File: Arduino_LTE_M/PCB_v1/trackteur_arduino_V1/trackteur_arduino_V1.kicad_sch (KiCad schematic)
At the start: 17 parts, among them J1 rPi_HDR, J2 DC/DC, J3 BATT_CAR, J4 MicroSD_Breakout, Q1 2N3904, U1 LD1117S33TR_SOT223

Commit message: update PCB
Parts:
- added H1, H2, H3: MountingHole, MountingHole:MountingHole_2.7mm_M2.5, symbol Mechanical:MountingHole
- added J5: Conn_02x02_Counter_Clockwise, Connector_PinHeader_2.54mm:PinHeader_2x02_P2.54mm_Vertical, symbol Connector_Generic:Conn_02x02_Counter_Clockwise
- added J6: Conn_01x06, Connector_PinHeader_2.54mm:PinHeader_1x06_P2.54mm_Vertical, symbol Connector_Generic:Conn_01x06
- added TP1: +5V, Connector_PinHeader_2.54mm:PinHeader_1x01_P2.54mm_Vertical, symbol Connector:TestPoint
- added TP2: GND, Connector_PinHeader_2.54mm:PinHeader_1x01_P2.54mm_Vertical, symbol Connector:TestPoint
- added TP3: +3.3V, Connector_PinHeader_2.54mm:PinHeader_1x01_P2.54mm_Vertical, symbol Connector:TestPoint
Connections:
- net +3.3V: now also TP3.1
- net +5V: now also J6.1 (Pin_1), TP1.1
- net GND: now also J6.6 (Pin_6), TP2.1
- net D7: now reaches A1.10 (D7)
- net D7: now also J6.4 (Pin_4)
- net D10: now reaches A1.13 (D10)
- net D10: now also J6.5 (Pin_5)
- net A0: now reaches A1.19 (A0)
- net A0: now also J5.4 (Pin_4)
- net A1: now reaches A1.20 (A1)
- net A1: now also J5.3 (Pin_3)
- net A2: now reaches A1.21 (A2)
- net A2: now also J5.2 (Pin_2)
- net A3: now reaches A1.22 (A3)
- net A3: now also J5.1 (Pin_1)
- net D5: now reaches A1.8 (D5)
- net D5: now also J6.2 (Pin_2)
- net D9: now reaches A1.9 (D6)
- net D9: now also J6.3 (Pin_3)

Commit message: Fichiers de fabrication
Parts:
- J3: footprint Connector_Wire:SolderWire-0.75sqmm_1x02_P7mm_D1.25mm_OD3.5mm -> Connector_Wire:SolderWire-2.5sqmm_1x02_P7.2mm_D2.4mm_OD3.6mm
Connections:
- net A0: now also J5.3 (Pin_3); no longer J5.4 (Pin_4)
- net A1: now also J5.4 (Pin_4); no longer J5.3 (Pin_3)
- net A2: now also J5.1 (Pin_1); no longer J5.2 (Pin_2)
- net A3: now also J5.2 (Pin_2); no longer J5.1 (Pin_1)
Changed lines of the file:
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@@
     )
   )
-  (global_label "A2" (shape bidirectional) (at 137.16 120.65 180) (fields_autoplaced)
+  (global_label "A3" (shape bidirectional) (at 137.16 120.65 180) (fields_autoplaced)
     (effects (font (size 1.27 1.27)) (justify right))
     (property "Intersheetrefs" "${INTERSHEET_REFS}" (at 130.7654 120.65 0)
@@
     )
   )
-  (global_label "A3" (shape bidirectional) (at 137.16 118.11 180) (fields_autoplaced)
+  (global_label "A2" (shape bidirectional) (at 137.16 118.11 180) (fields_autoplaced)
     (effects (font (size 1.27 1.27)) (justify right))
     (property "Intersheetrefs" "${INTERSHEET_REFS}" (at 130.7654 118.11 0)
@@
     )
   )
-  (global_label "A0" (shape bidirectional) (at 149.86 118.11 0) (fields_autoplaced)
+  (global_label "A1" (shape bidirectional) (at 149.86 118.11 0) (fields_autoplaced)
     (effects (font (size 1.27 1.27)) (justify left))
     (property "Intersheetrefs" "${INTERSHEET_REFS}" (at 156.2546 118.11 0)
@@
     )
   )
-  (global_label "A1" (shape bidirectional) (at 149.86 120.65 0) (fields_autoplaced)
+  (global_label "A0" (shape bidirectional) (at 149.86 120.65 0) (fields_autoplaced)
     (effects (font (size 1.27 1.27)) (justify left))
     (property "Intersheetrefs" "${INTERSHEET_REFS}" (at 156.2546 120.65 0)
@@
       (effects (font (size 1.27 1.27)))
     )
-    (property "Footprint" "Connector_Wire:SolderWire-0.75sqmm_1x02_P7mm_D1.25mm_OD3.5mm" (at 26.67 41.91 0)
-      (effects (font (size 1.27 1.27)) hide)
-    )
+    (property "Footprint" "Connector_Wire:SolderWire-2.5sqmm_1x02_P7.2mm_D2.4mm_OD3.6mm" (at 26.67 41.91 0)
+      (effects (font (size 1.27 1.27)) hide)
+    )

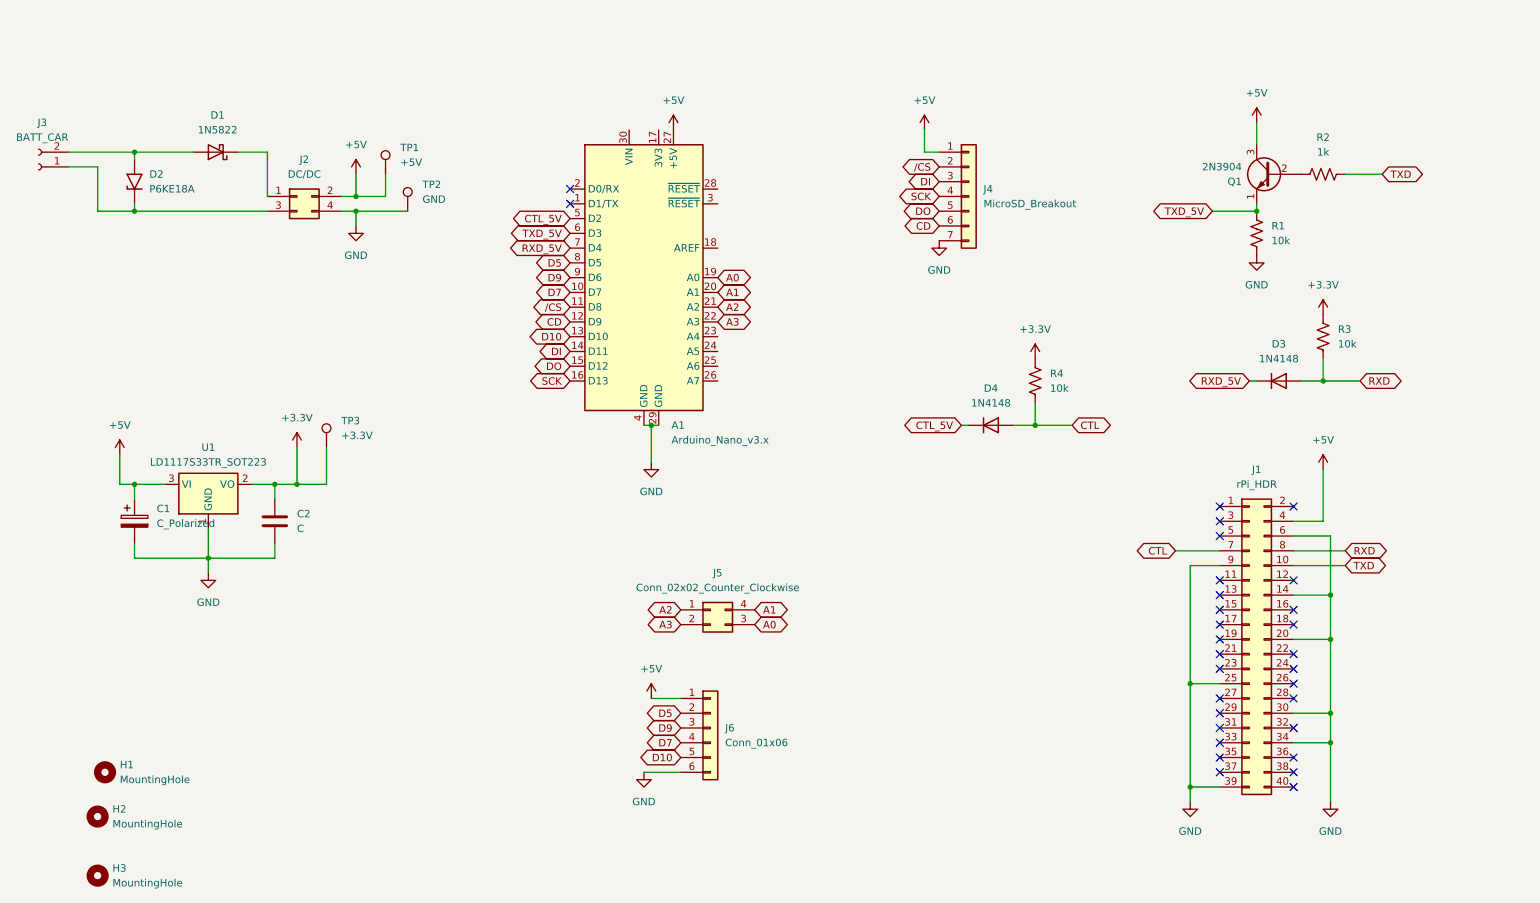
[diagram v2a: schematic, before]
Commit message: LTE send dummy gps working and new pcb
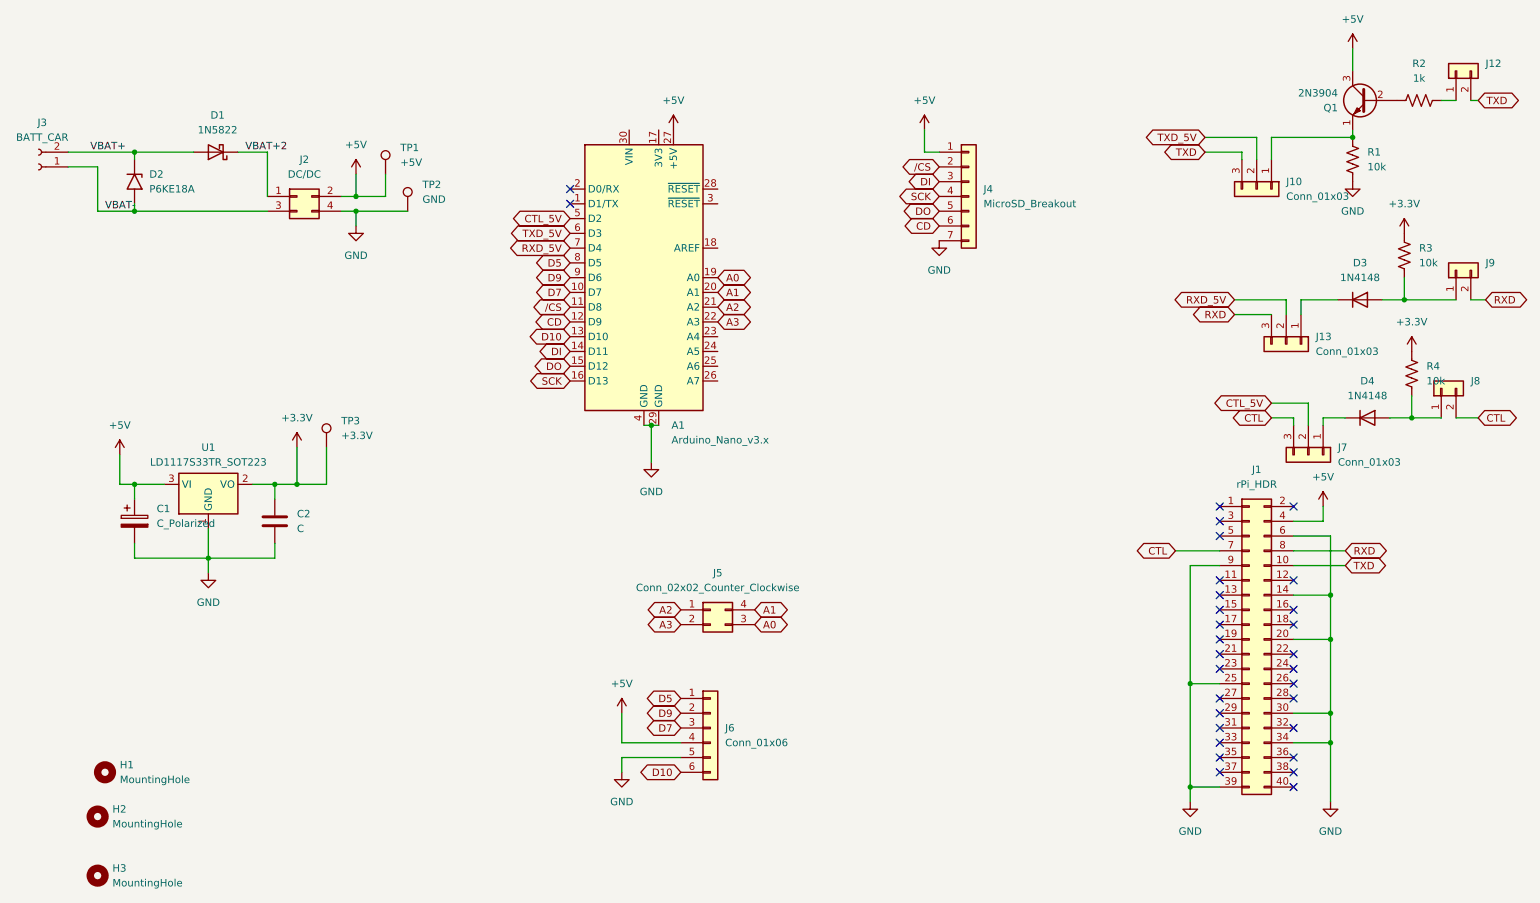
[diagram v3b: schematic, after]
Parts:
- added J10, J13, J7: Conn_01x03, Connector_PinHeader_2.54mm:PinHeader_1x03_P2.54mm_Vertical, symbol Connector_Generic:Conn_01x03
- added J12, J8, J9: Conn_01x02, Connector_PinHeader_2.54mm:PinHeader_1x02_P2.54mm_Vertical, symbol Connector_Generic:Conn_01x02
- J3: footprint Connector_Wire:SolderWire-2.5sqmm_1x02_P7.2mm_D2.4mm_OD3.6mm -> footprint_project:TE_282837-2
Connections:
- net +5V: now also J6.4 (Pin_4); no longer J6.1 (Pin_1)
- net CTL: now also J7.3 (Pin_3), J8.2 (Pin_2); no longer D4.2 (A), R4.1
- net CTL_5V: now also J7.2 (Pin_2); no longer D4.1 (K)
- net D10: now also J6.6 (Pin_6); no longer J6.5 (Pin_5)
- net D5: now also J6.1 (Pin_1); no longer J6.2 (Pin_2)
- net D7: now also J6.3 (Pin_3); no longer J6.4 (Pin_4)
- net D9: now also J6.2 (Pin_2); no longer J6.3 (Pin_3)
- net GND: now also J6.5 (Pin_5); no longer J6.6 (Pin_6)
- net RXD: now also J13.3 (Pin_3), J9.2 (Pin_2); no longer D3.2 (A), R3.1
- net RXD_5V: now also J13.2 (Pin_2); no longer D3.1 (K)
- net TXD: now also J10.3 (Pin_3), J12.2 (Pin_2); no longer R2.2
- net TXD_5V: now also J10.2 (Pin_2); no longer Q1.1 (E), R1.2
- net VBAT+2: now reaches D1.1 (K), J2.1 (Pin_1)
- net VBAT-: now reaches J2.3 (Pin_3), J3.1 (Pin_1)
- net VBAT-: now also D2.2 (A2); no longer D2.1 (A1)
- net VBAT+: now reaches D1.2 (A), J3.2 (Pin_2)
- net VBAT+: now also D2.1 (A1); no longer D2.2 (A2)
- new net: D3.1 (K), J13.1 (Pin_1)
- new net: D3.2 (A), J9.1 (Pin_1), R3.1
- new net: D4.1 (K), J7.1 (Pin_1)
- new net: J12.1 (Pin_1), R2.2
- new net: J10.1 (Pin_1), Q1.1 (E), R1.2
- new net: D4.2 (A), J8.1 (Pin_1), R4.1
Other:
- moved on the sheet: D2, D3, D4, Q1, R1, R2, R3, R4
